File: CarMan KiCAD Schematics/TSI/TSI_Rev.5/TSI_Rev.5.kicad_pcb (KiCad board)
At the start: 2 copper layers, 203.2 x 165.1 mm, 259 parts, among them IC1 TS431ILT, IC4 TS431ILT, J1 J1, J10 J10, J11 J11, J12 J12, J13 Conn_01x01, J13.1 Conn_01x06, J13.2 Conn_01x06, J14 J14, J15 J15, J16 J16, J17 J17, J18 J18, J19 J19, J2 Current_Sensor, J20 J20, J21 J21, J22 J22, J23 J23, J24 Conn_01x01, J25 Conn_01x01, J26 J26, J27 J27, J28 Conn_01x01, J29 J29, J3 J3, J30 J23, J4 J4, J5 J5, J6 J6, J7 J7, J8 J8, J9 J9, K1 APAN3105, K2 G5LE-1-E, K3 SFS2-DC24V, K4 SFS2-DC24V, Q1 ZVP1320F, Q11 TN2130K1-G, Q2 MMBF170, Q3 ZVP1320F, Q5 SI1302DL-T1-E3, SW1 TS5A3159DBVT, U1 RDE03110S12, U10 MC7805BDTRKG, U11 TLP293, U12 REF3033, U13 TLP293, U14 Bottom Left, U15 Top Left, U16 TS372CDT, U17 Top Right, U18 MCP6004, U19 74HC00, U2 Bottom Right, U20 TLP293, U21 MCP6004, U22 MCP23016-I_SO, U23 DAC5574IDGS, U24 TLP293, U25 NCD9830DBR2G, U26 MCP6004, U29 SN74LVC1G08DCKR, U3 TS912, U30 TLP293, U31 TLP293, U32 TLP293, U34 TLP293, U35 MCP6004, U37 TLP293, U4 ACPL-C870, U40 MCP6004, U41 PDQ10-Q24-D5-D, U42 LT1763CS8-3.3PBF, U48 TLP293, U49 TLP293, U5 SI8600AB-B-IS, U6 TS912, U7 MCP6004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

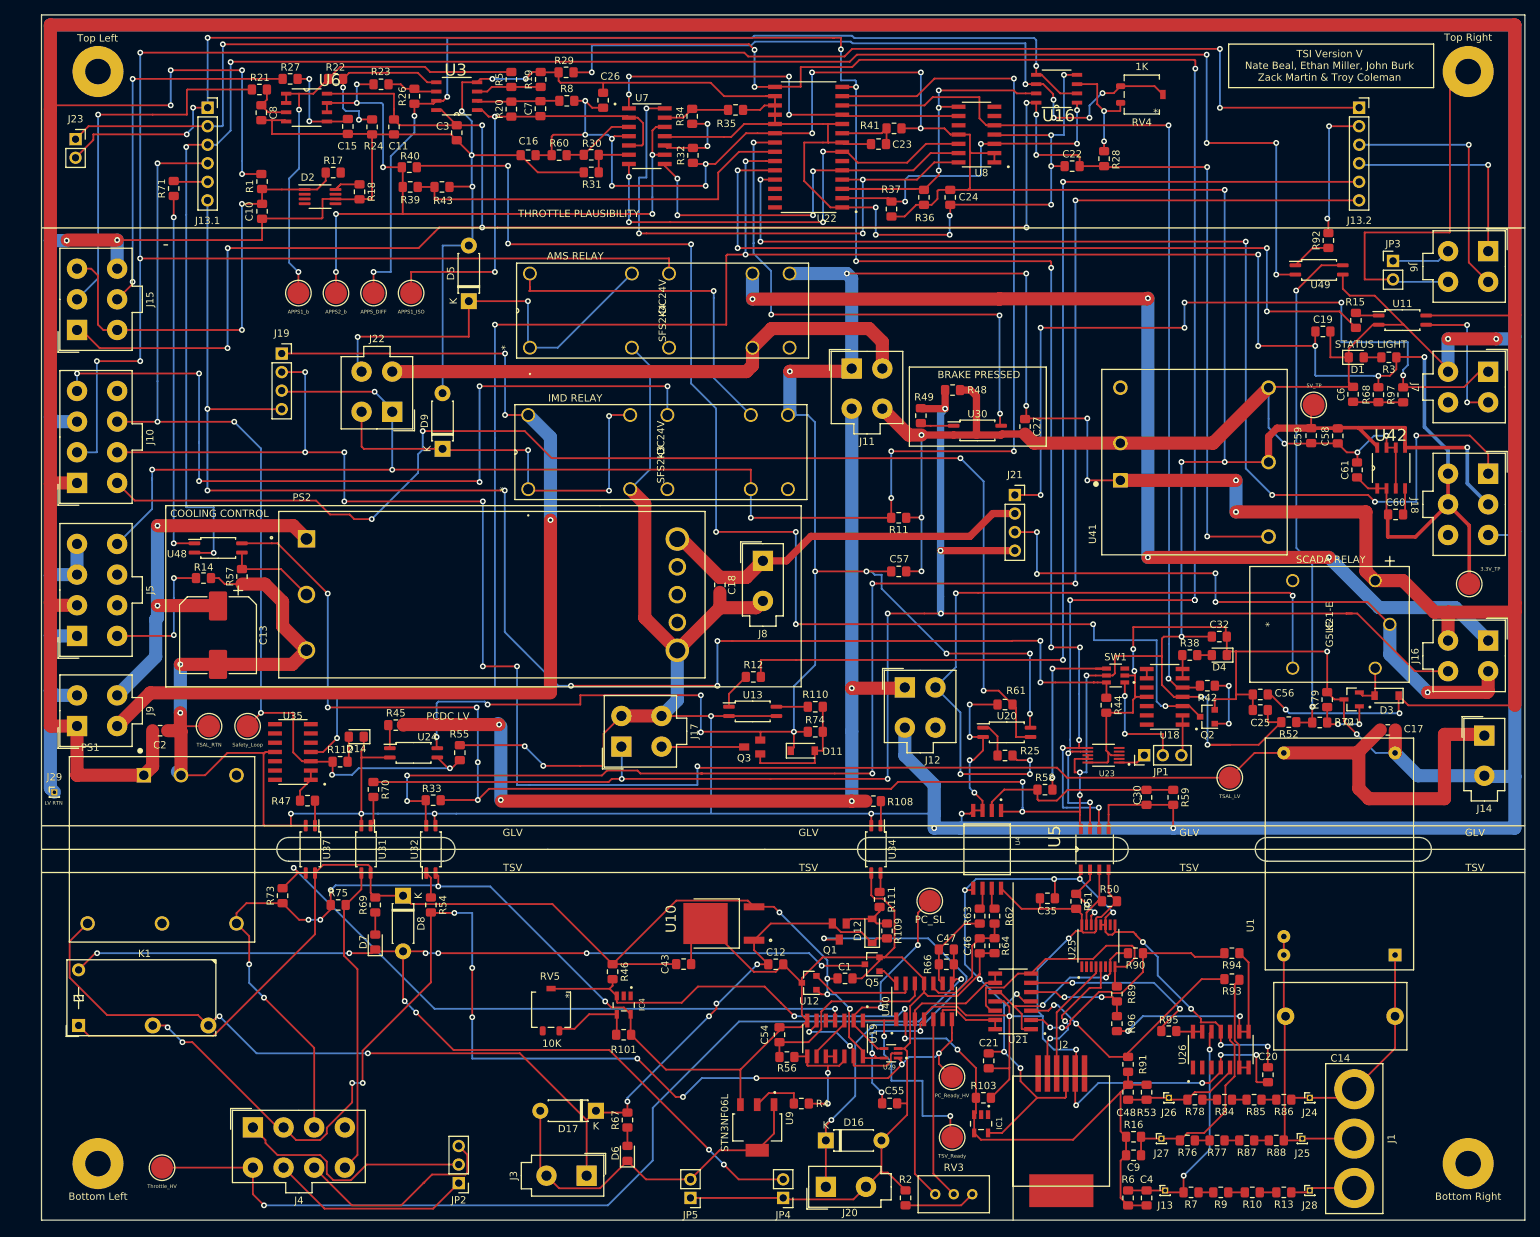
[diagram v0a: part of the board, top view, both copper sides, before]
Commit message: Changed TSI to ground pour
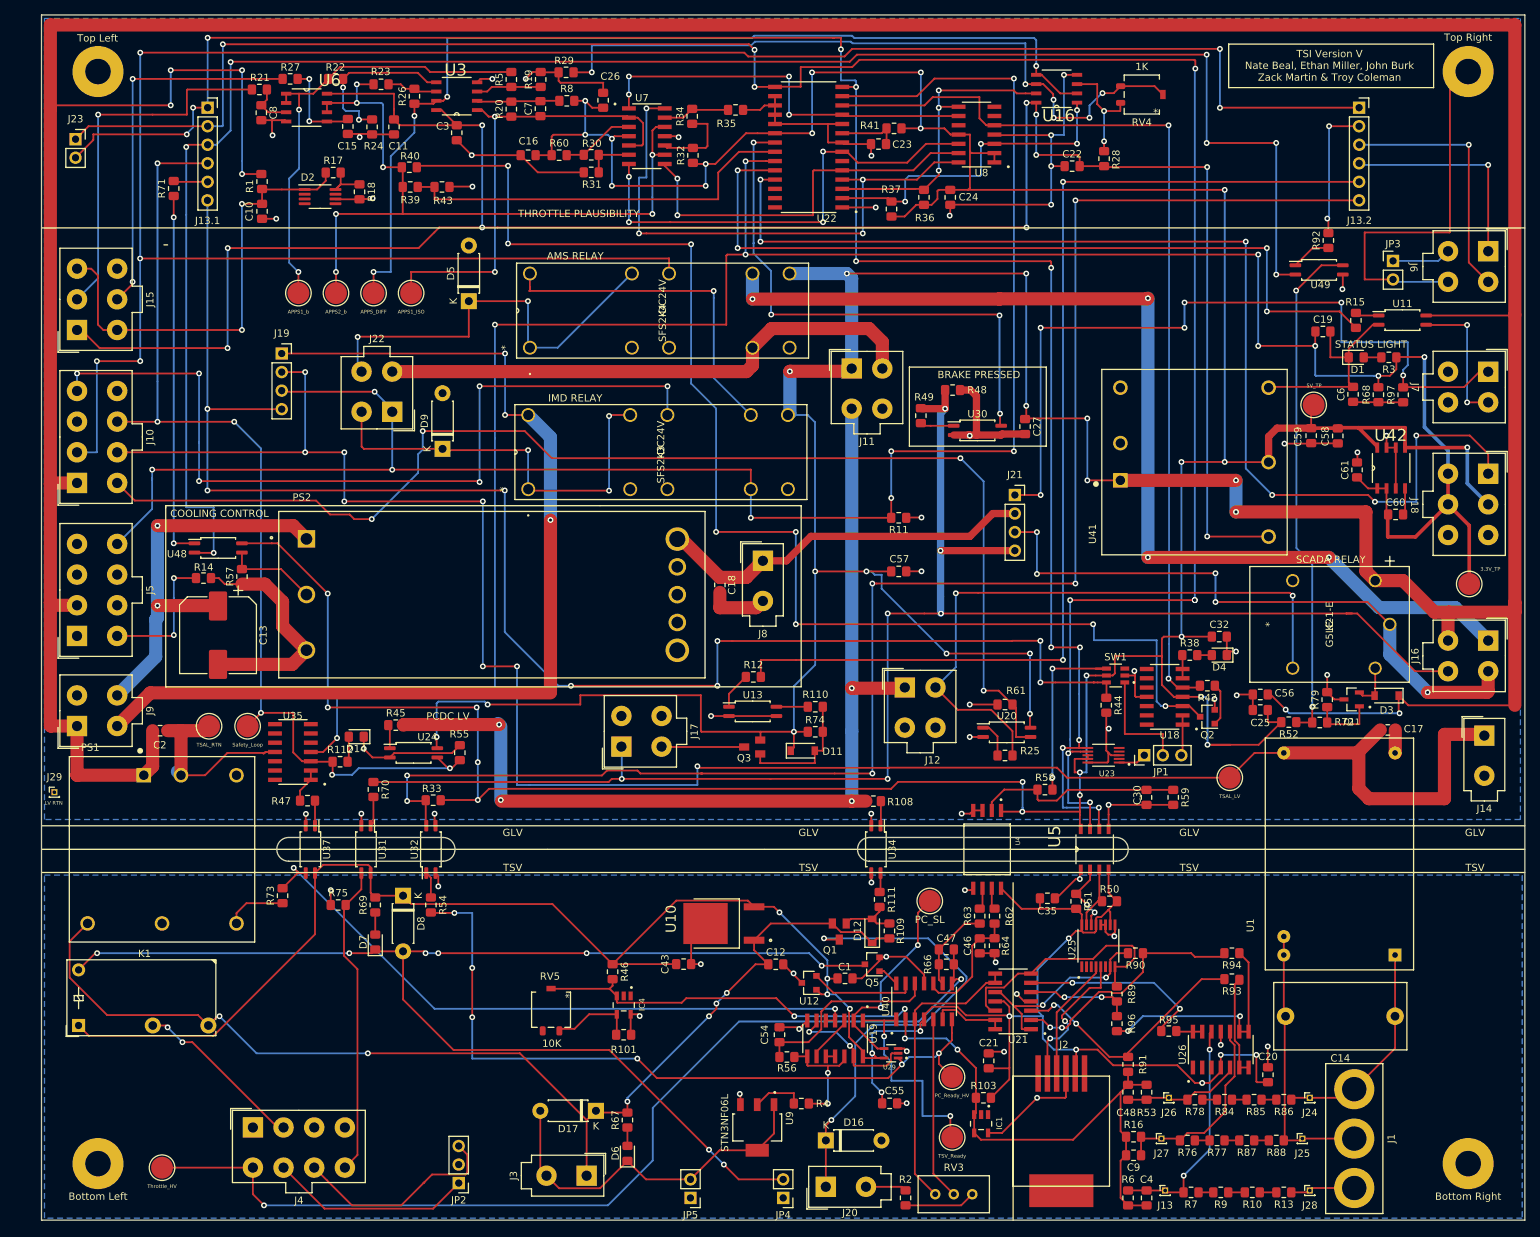
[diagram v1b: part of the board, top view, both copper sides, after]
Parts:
- moved R109 0.33 mm to (216.3, 178.3)
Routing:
- net /AIRS-: track 1557.2 -> 369.5 mm, vias 43 -> 39
- net /DC_RELAY-: track 444.2 -> 100.9 mm, vias 19 -> 20
- net /IGNI_VCC: track 67.8 -> 23.7 mm, vias 4 -> 2
- net /GEN_Fault_LED: track 97.7 -> 86.7 mm, vias 5 -> 2
- net Net-(Q2-Pad1): track 9.03 -> 5.85 mm, vias 2 -> 0
- net /PCDC_Circuit/PC_Ready_HV: track 104.2 -> 102.1 mm, vias 8 -> 6
- net /5HV: track 314.5 -> 312.8 mm, vias 14 -> 13
- net Net-(D2-Pad8): track 4.31 -> 5.93 mm
- net /1.24V_REF: track 127.1 -> 125.8 mm
- net (no net): track 1.27 -> 0.00 mm
- net /PC_RELAY+: track 156.2 -> 156.7 mm
- net /24V: track 862.7 -> 862.5 mm, vias 24 -> 22
- net Net-(R32-Pad2): vias 2 -> 0
- net Net-(Q11-Pad1): vias 2 -> 0
- net Net-(JP1-Pad2): vias 2 -> 0
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- added copper zone on B.Cu, net /AIRS-
- added copper zone on B.Cu, net /DC_RELAY-
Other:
- outline, holes or cut-outs redrawn

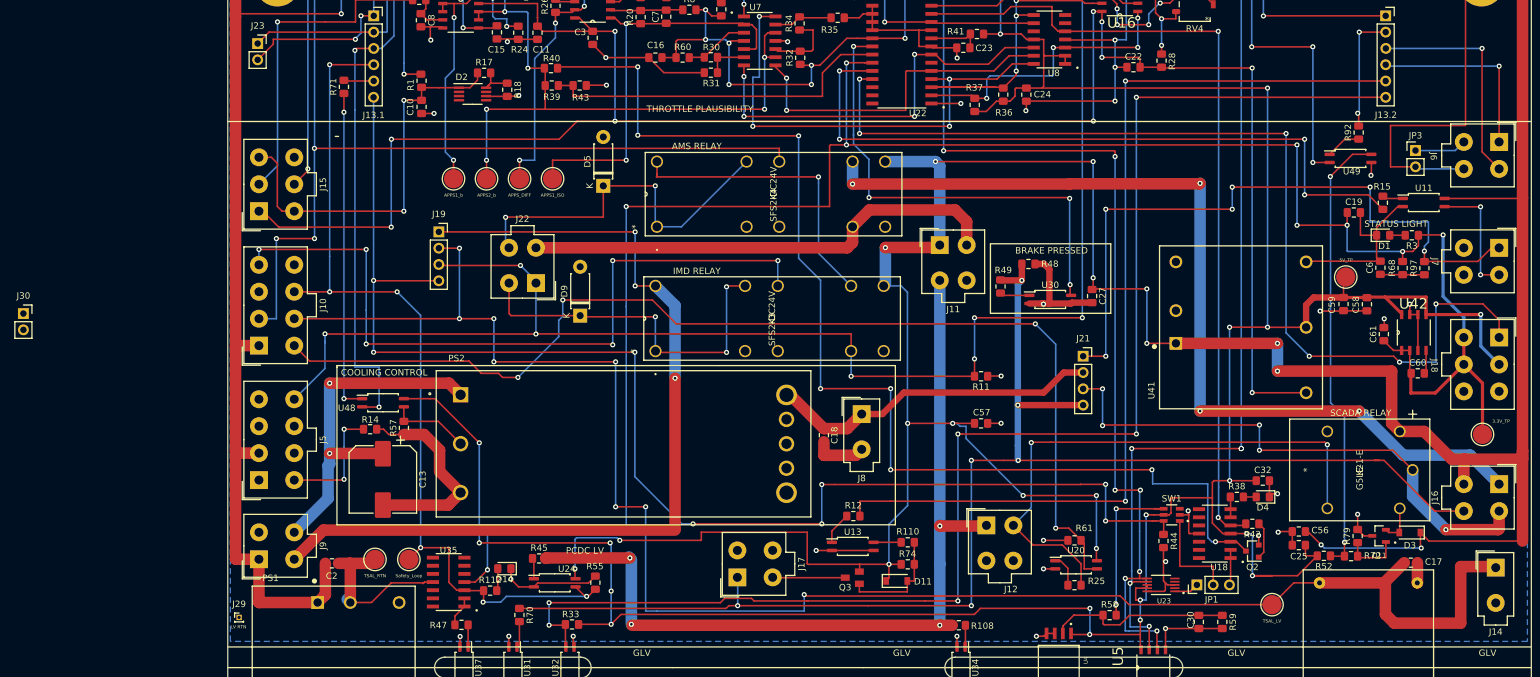
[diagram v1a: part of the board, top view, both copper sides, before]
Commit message: TSI PCB Aesthetic changes
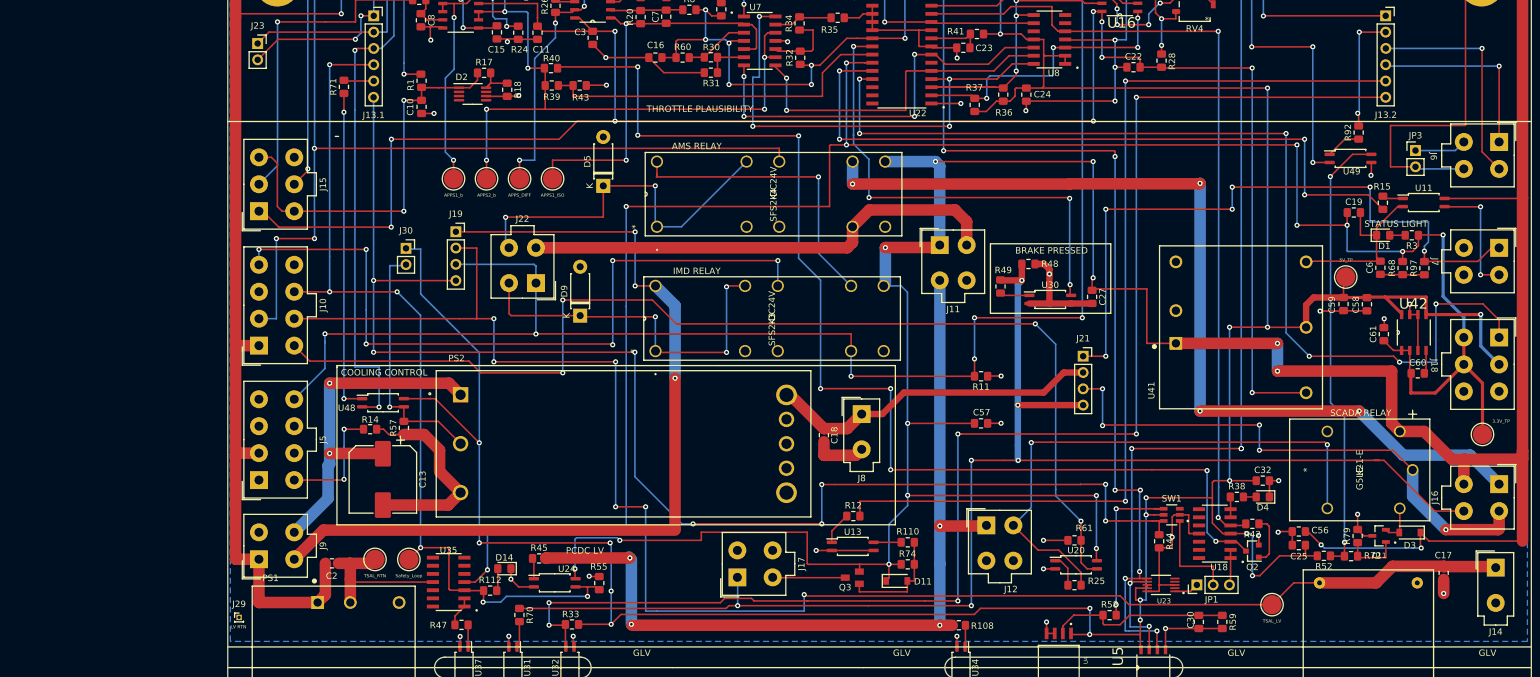
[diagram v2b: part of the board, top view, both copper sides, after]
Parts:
- moved J30 60.5 mm to (128.0, 101.8)
- moved C17 5.35 mm to (289.7, 152.4), turned to 270 degrees
- moved J19 2.65 mm to (135.7, 99.2)
- moved R44 0.67 mm to (245.4, 147.5)
- moved R55 0.61 mm to (158.1, 154.0)
- moved C27 0.12 mm to (234.9, 109.4)
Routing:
- net /5V: track 535.0 -> 569.4 mm, vias 27 -> 28
- net /CAN_GLV_POWER/Cooling_power: track 12.5 -> 39.4 mm, vias 0 -> 1
- net /TSAL: track 270.7 -> 253.0 mm, vias 8 -> 6
- net /AIRS-: track 369.5 -> 364.9 mm, vias 39 -> 40
- net /Throttle_SEL: track 209.5 -> 212.3 mm
- net /SL1_In: track 142.6 -> 139.9 mm
- net Net-(Q2-Pad1): track 5.85 -> 7.92 mm
- net /Safety_Loop: track 140.6 -> 142.6 mm
- net /24V: track 862.5 -> 864.3 mm, vias 22 -> 19
- net /Gen_Fault_EPAL: track 172.5 -> 174.1 mm
- net /IMD_Status: track 246.2 -> 245.1 mm, vias 8 -> 7
- net /GEN_Fault_LED: track 86.7 -> 85.9 mm

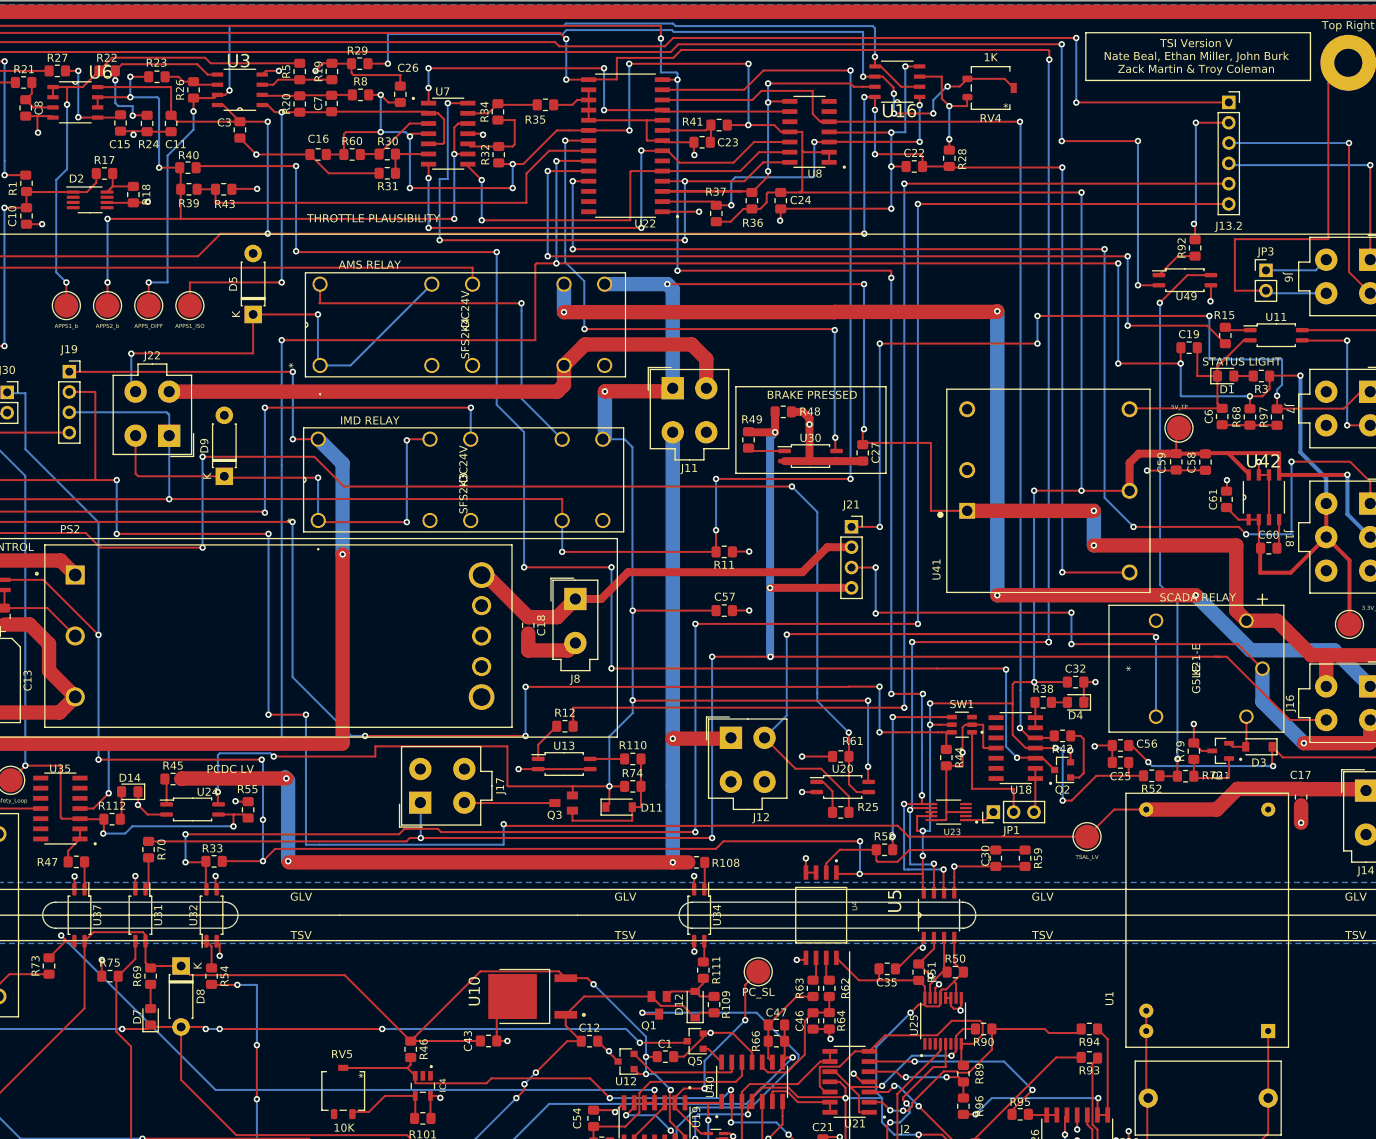
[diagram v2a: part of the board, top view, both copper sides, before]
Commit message: Changed order of names on TSI Board
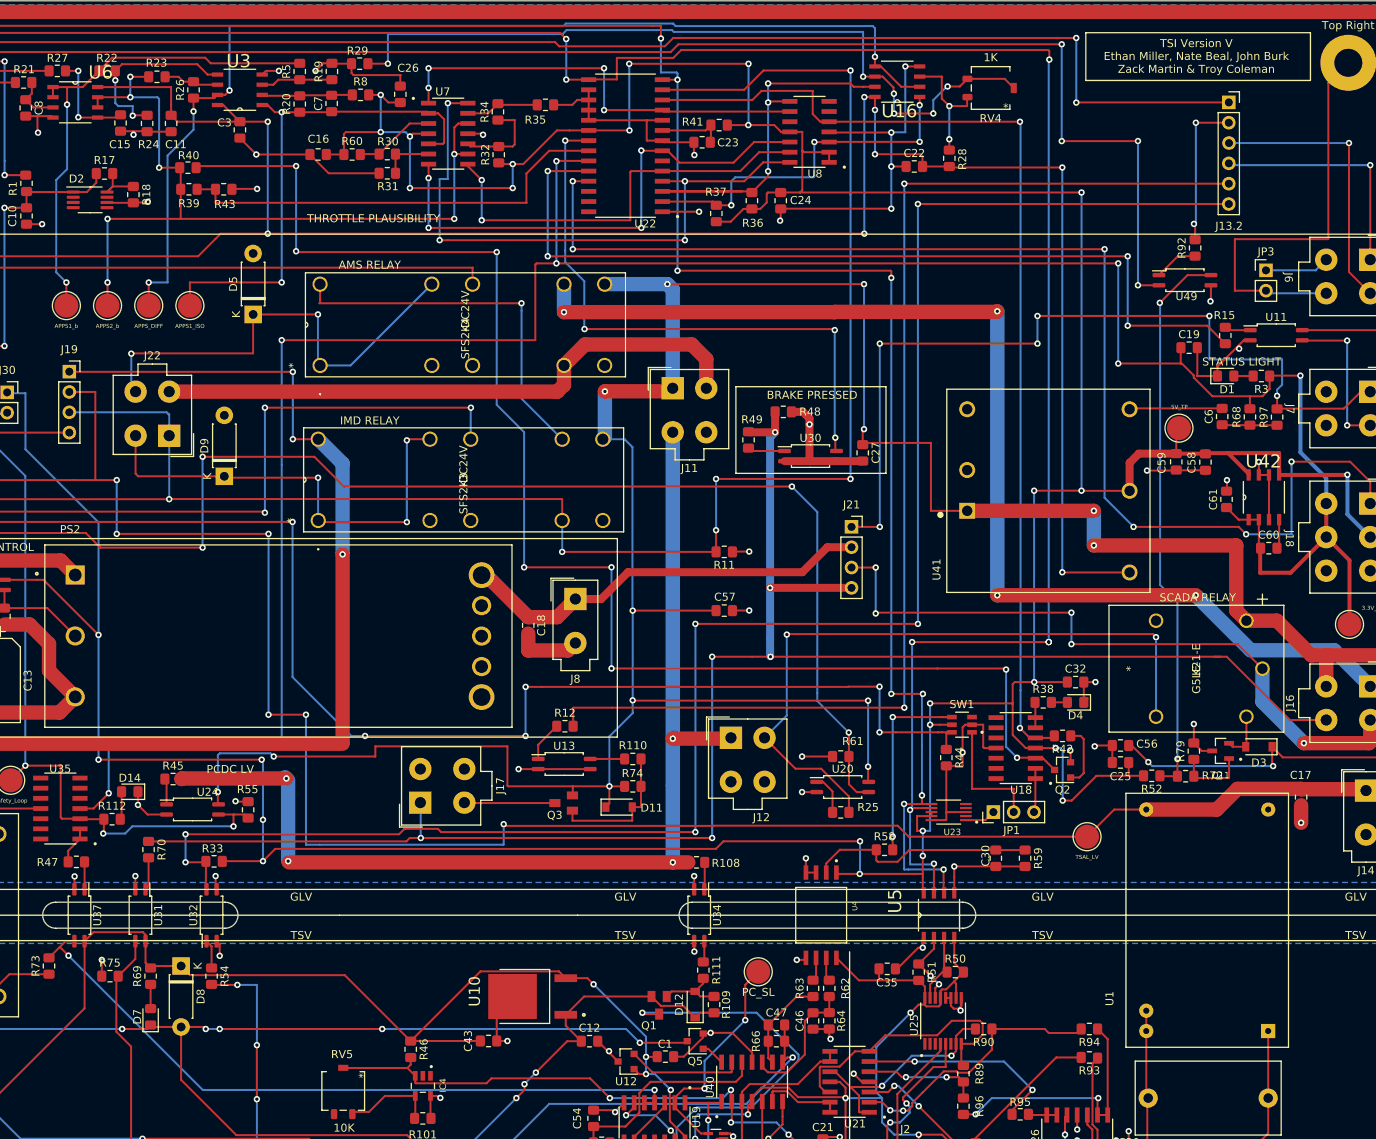
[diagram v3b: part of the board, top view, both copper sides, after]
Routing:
- net /AIRS-: track 364.9 -> 361.0 mm, vias 40 -> 41
- net /3.3V: track 313.6 -> 311.4 mm, vias 9 -> 7
- net /PCDC_Circuit/Safety_Loop_HV: track 90.0 -> 88.7 mm
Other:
- board text added: "TSI Version V Ethan Miller, Nate Beal, John Burk Zack Martin & Troy Coleman"
- board text removed: "TSI Version V Nate Beal, Ethan Miller, John Burk Zack Martin & Troy Coleman"
